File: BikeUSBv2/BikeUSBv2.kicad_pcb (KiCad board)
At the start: 2 copper layers, 43.6 x 25.5 mm, 52 parts, among them J1 TYPE-C-31-M-16, J2 Conn_01x02_Female, Q1 SSM3J332R,LF, Q2 SSM3J332R,LF, SW1 SW_Push, SW2 SW_Push, U1 TPS63020DSJR, U2 ATtiny1616-M

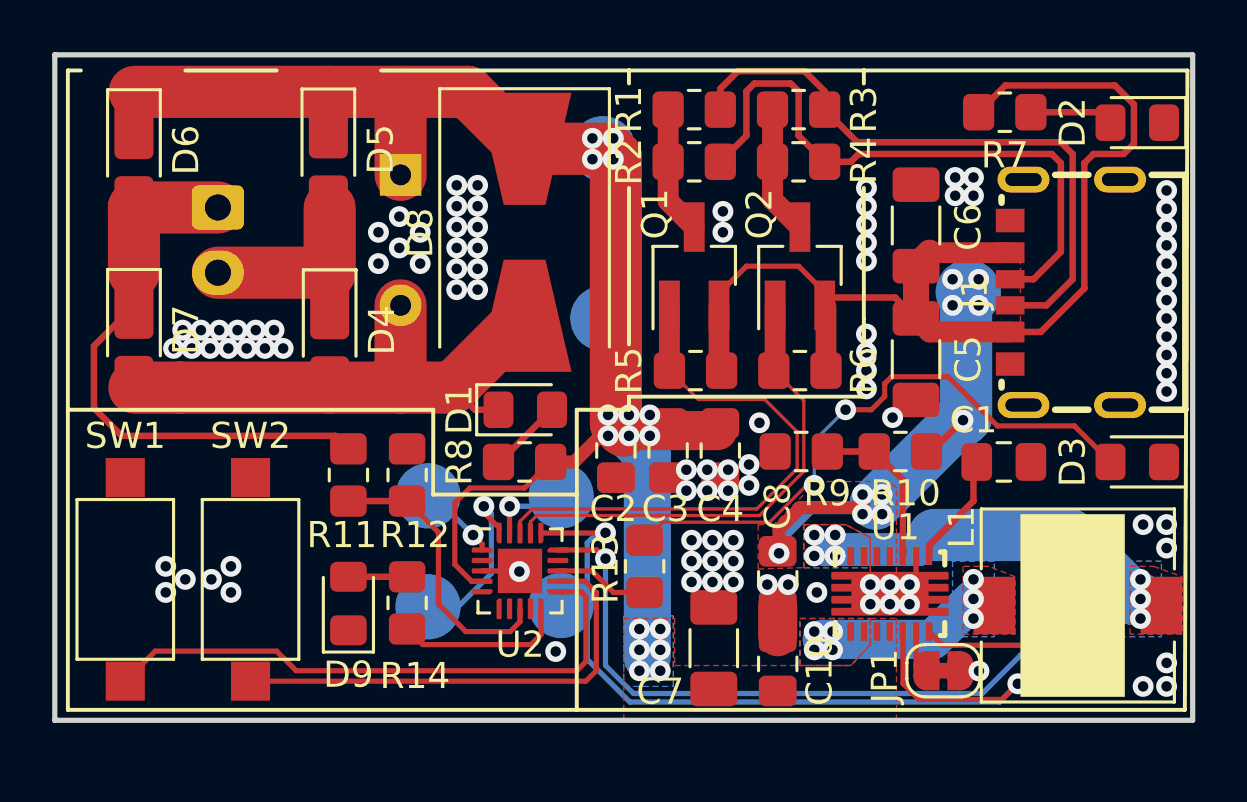
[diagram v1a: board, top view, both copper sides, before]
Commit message: added footprint for clamping diode if needed
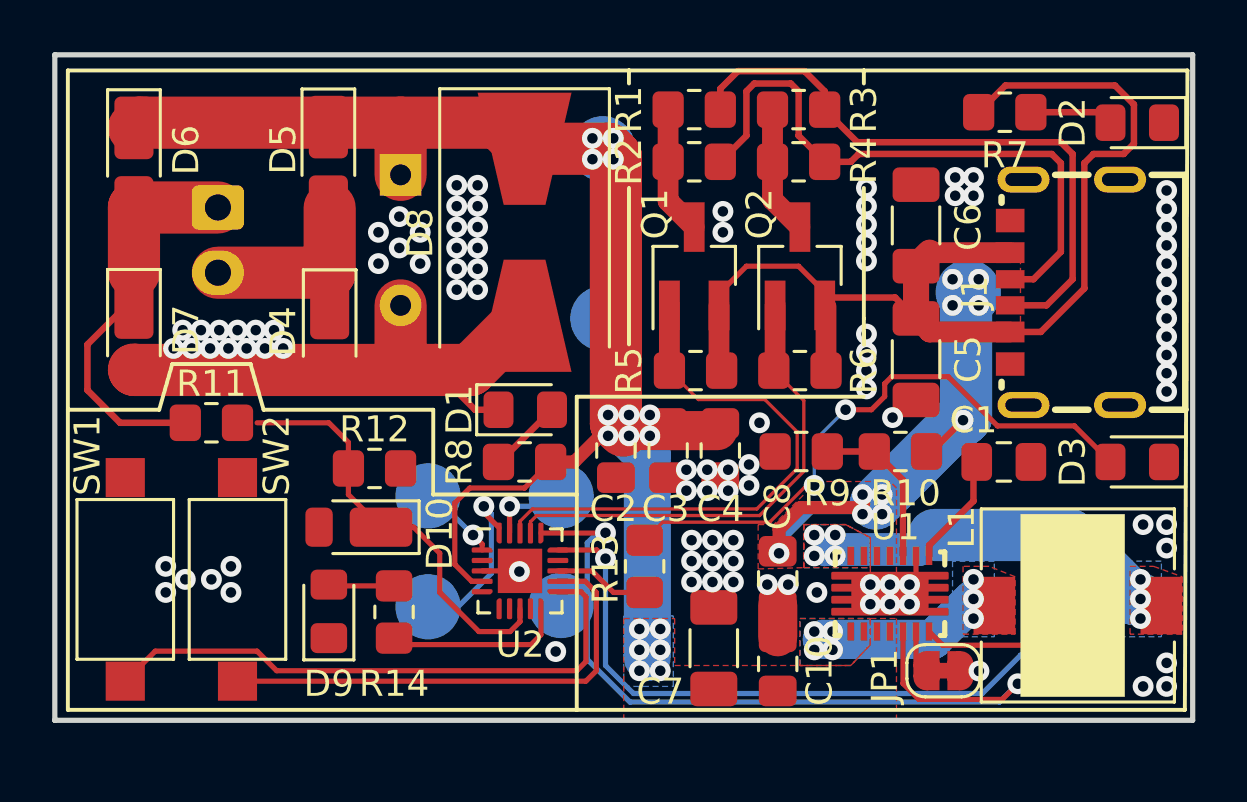
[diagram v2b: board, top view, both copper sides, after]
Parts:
- added D10: CMS04(TE12L,Q,M), Diode_SMD:D_PowerDI-123, F.Cu at (121.7, 100.5)
- moved R11 5.62 mm to (116.0, 96.5), turned to 180 degrees
- moved R12 1.27 mm to (122.2, 98.2), turned to 180 degrees
- moved D9 0.81 mm to (120.5, 103.7)
- moved R14 0.61 mm to (123.0, 103.8)
- moved SW2 0.50 mm to (117.0, 102.5)
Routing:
- net /AC2: track 20.6 -> 14.1 mm
- net / AC_LV: track 10.9 -> 16.1 mm
- net VCC: track 57.4 -> 55.9 mm

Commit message: reduced component count
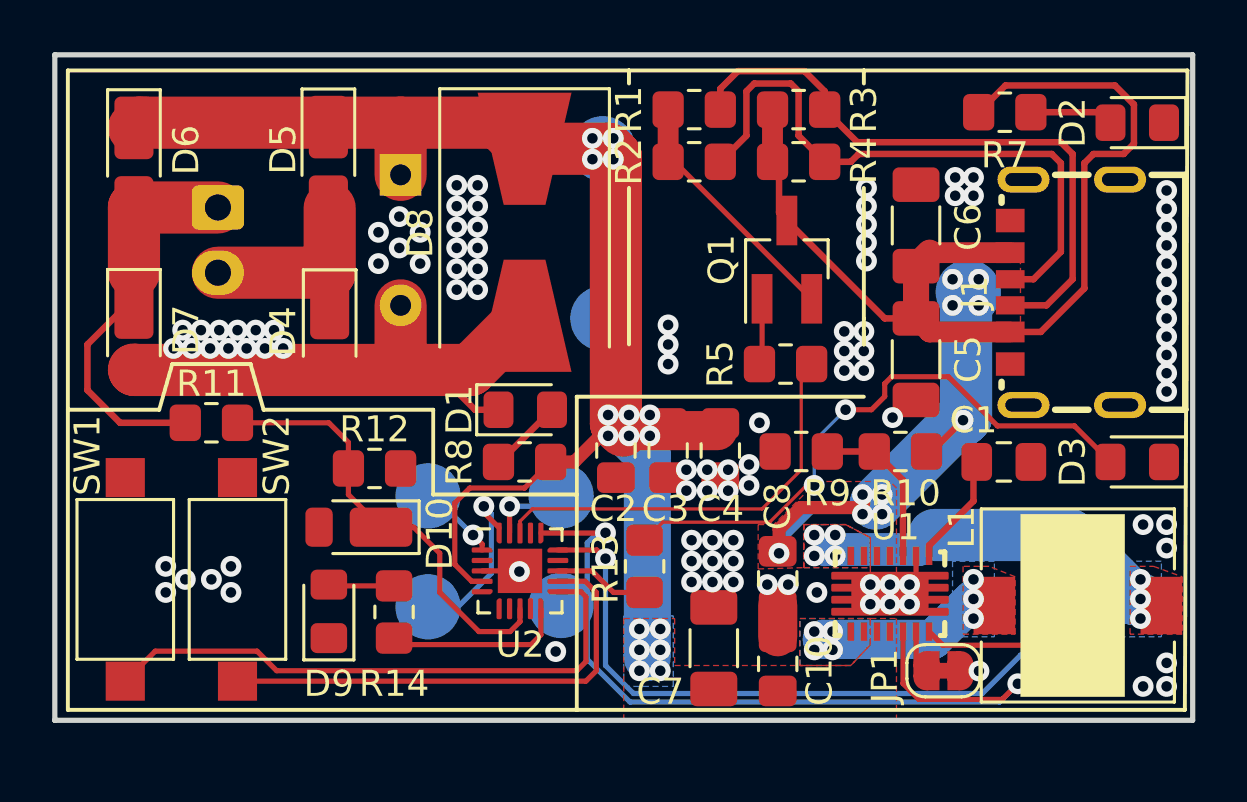
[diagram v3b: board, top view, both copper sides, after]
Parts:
- removed Q2: SSM3J332R,LF, Package_TO_SOT_SMD:SOT-23_Handsoldering
- removed R6: 47k, Resistor_SMD:R_0805_2012Metric_Pad1.20x1.40mm_HandSolder
- Q1: value SSM3J332R,LF -> Q_NPN_BEC
- moved Q1 3.56 mm to (138.1, 90.2)
- moved R5 3.46 mm to (138.0, 94.2), turned to 180 degrees
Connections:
- Q1 pad 1: /CCR1 -> Net-(Q1-B)
- Q1 pad 2: +5V -> Net-(Q1-E)
- Q1 pad 3: Net-(Q1-D) -> +5V
- R1 pad 2: Net-(Q1-D) -> Net-(Q1-E)
- R2 pad 2: Net-(Q1-D) -> Net-(Q1-E)
- R3 pad 2: Net-(Q2-D) -> +5V
- R4 pad 2: Net-(Q2-D) -> +5V
- R5 pad 1: /CCR1 -> /CCR
- R5 pad 2: +5V -> Net-(Q1-B)
- U2 pad 17: /CCR2 -> unconnected-(U2-PC2-Pad17)
- U2 pad 18: /CCR1 -> /CCR
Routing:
- net /CCR1: track 21.7 -> 0.00 mm
- net /CCR2: track 18.5 -> 0.00 mm
- net /CCR: track 0.00 -> 16.2 mm
- net Net-(Q1-E): track 0.00 -> 9.67 mm
- net Net-(Q2-D): track 4.93 -> 0.00 mm
- net Net-(Q1-D): track 4.91 -> 0.00 mm
- net Net-(Q1-B): track 0.00 -> 2.64 mm
- net +5V: track 62.0 -> 59.5 mm
- net / AC_LV: track 16.1 -> 16.8 mm
- net GND: vias 106 -> 109

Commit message: better layout
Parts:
- added C11: 100n, Capacitor_SMD:C_0805_2012Metric_Pad1.18x1.45mm_HandSolder, F.Cu at (140.8, 90.5)
- moved R1 2.14 mm to (133.8, 86.5), turned to -90 degrees
- moved R3 2.14 mm to (137.8, 86.5), turned to -90 degrees
- moved TP3 2.06 mm to (131.5, 88.0)
- moved Q1 1.67 mm to (136.8, 91.3), turned to 180 degrees
- moved R2 1.25 mm to (135.8, 86.5), turned to -90 degrees
- moved R4 1.25 mm to (139.8, 86.5), turned to -90 degrees
- moved TP2 1.12 mm to (131.5, 93.5)
- moved R5 0.75 mm to (137.2, 94.2), turned to 0 degrees
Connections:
- R1 pad 2: Net-(Q1-E) -> +5V
- R2 pad 2: Net-(Q1-E) -> +5V
- R3 pad 2: +5V -> Net-(Q1-E)
- R4 pad 2: +5V -> Net-(Q1-E)
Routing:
- net Net-(Q1-E): track 9.67 -> 5.41 mm
- net +5V: track 59.5 -> 63.4 mm
- net Net-(J1-CC2): track 23.6 -> 20.3 mm
- net Net-(J1-CC1): track 23.9 -> 25.2 mm
- net /CCR: track 16.2 -> 17.1 mm
- net Net-(D3-A): track 23.2 -> 22.5 mm
- net GND: vias 109 -> 115

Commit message: stuff
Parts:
- moved REF** 1.00 mm to (137.0, 91.0)
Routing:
- net GND: vias 115 -> 121
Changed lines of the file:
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@@
   )
   (footprint "Symbol:KiCad-Logo2_6mm_SilkScreen" (layer "B.Cu")
-    (at 136 91 -90)
+    (at 137 91 -90)
     (descr "KiCad Logo")
     (tags "Logo KiCad")
@@
   (gr_line (start 130 107.5) (end 153.3 107.5)
     (stroke (width 0.15) (type default)) (layer "F.SilkS"))
+  (gr_rect (start 140.9 102.4) (end 143.1 103.7)
+    (stroke (width 0.2) (type solid)) (fill solid) (layer "B.Mask"))
   (gr_circle (center 137.75 101.5) (end 138.15 101.5)
     (stroke (width 0) (type solid)) (fill solid) (layer "B.Mask"))
@@
   (via (at 152.6 89.7) (size 0.8) (drill 0.4) (layers "F.Cu" "B.Cu") (free) (net 2))
   (via (at 115.6 92.95) (size 0.8) (drill 0.4) (layers "F.Cu" "B.Cu") (free) (net 2))
+  (via (at 148.5 93.5) (size 0.8) (drill 0.4) (layers "F.Cu" "B.Cu") (free) (net 2))
   (via (at 152.6 91.8) (size 0.8) (drill 0.4) (layers "F.Cu" "B.Cu") (free) (net 2))
   (via (at 126.2 90.6) (size 0.8) (drill 0.4) (layers "F.Cu" "B.Cu") (free) (net 2))
@@
   (via (at 152.6 90.4) (size 0.8) (drill 0.4) (layers "F.Cu" "B.Cu") (free) (net 2))
   (via (at 141.8 87.6) (size 0.8) (drill 0.4) (layers "F.Cu" "B.Cu") (free) (net 2))
+  (via (at 147.75 94.25) (size 0.8) (drill 0.4) (layers "F.Cu" "B.Cu") (free) (net 2))
   (via (at 134.4 102.6) (size 0.8) (drill 0.4) (layers "F.Cu" "B.Cu") (free) (net 2))
   (via (at 142.6 89.2) (size 0.8) (drill 0.4) (layers "F.Cu" "B.Cu") (free) (net 2))
@@
   (via (at 151.7 106.6) (size 0.8) (drill 0.4) (layers "F.Cu" "B.Cu") (free) (net 2))
   (via (at 152.6 87.6) (size 0.8) (drill 0.4) (layers "F.Cu" "B.Cu") (free) (net 2))
+  (via (at 148.5 95) (size 0.8) (drill 0.4) (layers "F.Cu" "B.Cu") (free) (net 2))
   (via (at 152.6 95.3) (size 0.8) (drill 0.4) (layers "F.Cu" "B.Cu") (free) (net 2))
   (via (at 140 94) (size 0.8) (drill 0.4) (layers "F.Cu" "B.Cu") (free) (net 2))
@@
   (via (at 137 96.5) (size 0.8) (drill 0.4) (layers "F.Cu" "B.Cu") (free) (net 2))
   (via (at 141.25 103.45) (size 0.8) (drill 0.4) (layers "F.Cu" "B.Cu") (net 2))
+  (via (at 142.5 94.5) (size 0.8) (drill 0.4) (layers "F.Cu" "B.Cu") (free) (net 2))
   (via (at 142.75 102.7) (size 0.8) (drill 0.4) (layers "F.Cu" "B.Cu") (net 2))
   (via (at 114.55 93.65) (size 0.8) (drill 0.4) (layers "F.Cu" "B.Cu") (free) (net 2))
+  (via (at 148.5 94.25) (size 0.8) (drill 0.4) (layers "F.Cu" "B.Cu") (free) (net 2))
   (via (at 133.5 94.25) (size 0.8) (drill 0.4) (layers "F.Cu" "B.Cu") (free) (net 2))
   (via (at 152.6 105.7) (size 0.8) (drill 0.4) (layers "F.Cu" "B.Cu") (free) (net 2))
   (via (at 136 101.8) (size 0.8) (drill 0.4) (layers "F.Cu" "B.Cu") (free) (net 2))
+  (via (at 143.25 94.5) (size 0.8) (drill 0.4) (layers "F.Cu" "B.Cu") (free) (net 2))
   (via (at 123.2 89.8) (size 0.8) (drill 0.4) (layers "F.Cu" "B.Cu") (free) (net 2))
   (via (at 140.75 94.75) (size 0.8) (drill 0.4) (layers "F.Cu" "B.Cu") (free) (net 2))
@@
   (via (at 129.192431 105.264334) (size 0.8) (drill 0.4) (layers "F.Cu" "B.Cu") (free) (net 2))
   (via (at 117.7 92.95) (size 0.8) (drill 0.4) (layers "F.Cu" "B.Cu") (free) (net 2))
+  (via (at 142.5 93.75) (size 0.8) (drill 0.4) (layers "F.Cu" "B.Cu") (free) (net 2))
   (via (at 144.5 87.1) (size 0.8) (drill 0.4) (layers "F.Cu" "B.Cu") (free) (net 2))
   (via (at 148.5 104) (size 0.8) (drill 0.4) (layers "F.Cu" "B.Cu") (net 2))
@@
   (via (at 145.410403 106.010403) (size 0.8) (drill 0.4) (layers "F.Cu" "B.Cu") (free) (net 2))
   (via (at 141.5 94.75) (size 0.8) (drill 0.4) (layers "F.Cu" "B.Cu") (free) (net 2))
-  (via (at 147.8 94.2) (size 0.8) (drill 0.4) (layers "F.Cu" "B.Cu") (free) (net 2))
   (via (at 125.4 89) (size 0.8) (drill 0.4) (layers "F.Cu" "B.Cu") (free) (net 2))
   (via (at 133.5 93.5) (size 0.8) (drill 0.4) (layers "F.Cu" "B.Cu") (free) (net 2))
@@
   (via (at 135 99.1) (size 0.8) (drill 0.4) (layers "F.Cu" "B.Cu") (free) (net 2))
   (via (at 152.6 88.3) (size 0.8) (drill 0.4) (layers "F.Cu" "B.Cu") (free) (net 2))
-  (segment (start 131.5 96.525) (end 131.775 96.8) (width 2) (layer "F.Cu") (net 3))
   (segment (start 113.0325 85.2) (end 113.2325 85) (width 2) (layer "F.Cu") (net 3))
   (segment (start 131.5 86.7) (end 131.5 96.525) (width 2) (layer "F.Cu") (net 3))
@@
       (pts
         (xy 146.8 102.4)
-        (xy 145.8 102)
-        (xy 144.8 102)
+        (xy 145.8 102.1)
+        (xy 144.8 102.1)
         (xy 144.8 104.6)
         (xy 146.8 104.6)

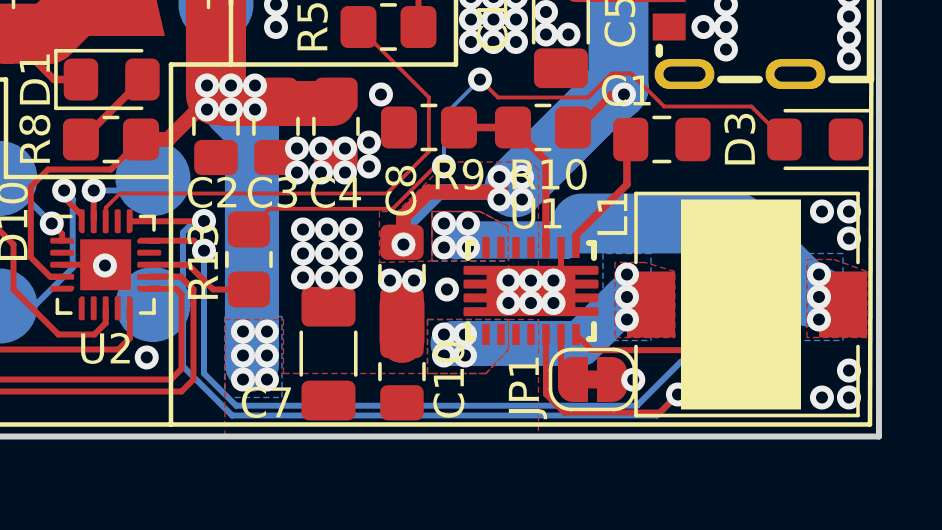
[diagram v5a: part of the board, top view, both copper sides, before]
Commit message: better inductor track layout
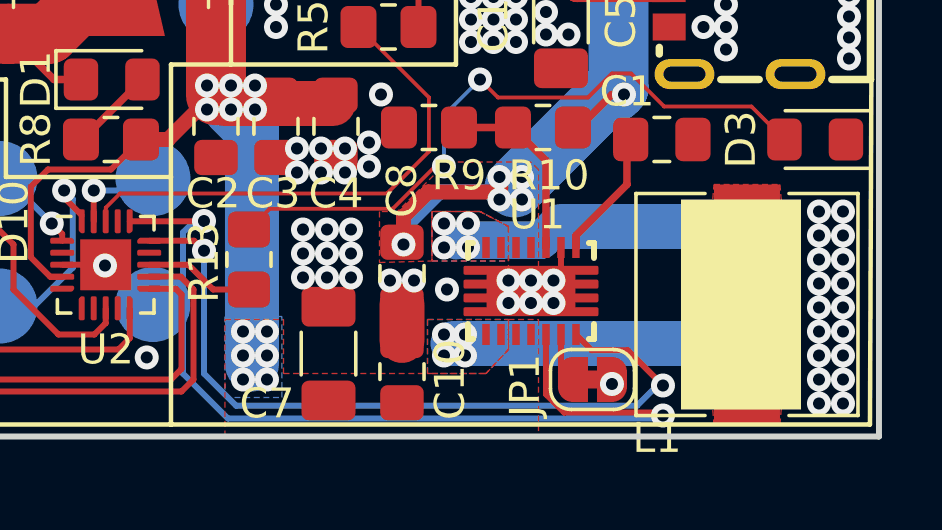
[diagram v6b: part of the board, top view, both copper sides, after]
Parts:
- turned L1 to 90 degrees
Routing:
- net /PG: track 29.9 -> 25.7 mm
- net Net-(L1-Pad2): track 13.5 -> 10.0 mm
- net Net-(L1-Pad1): track 6.44 -> 8.92 mm
- net /EN: track 32.2 -> 30.9 mm
- net GND: vias 121 -> 128
